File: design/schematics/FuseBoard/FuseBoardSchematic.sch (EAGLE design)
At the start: 11 parts

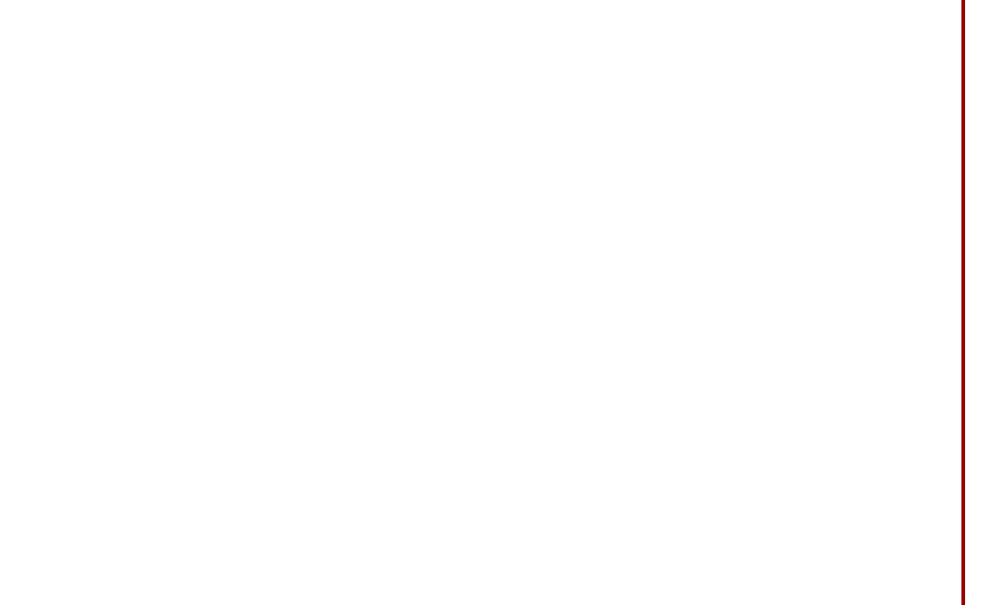
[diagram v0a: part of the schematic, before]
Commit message: Routed Fuse Board
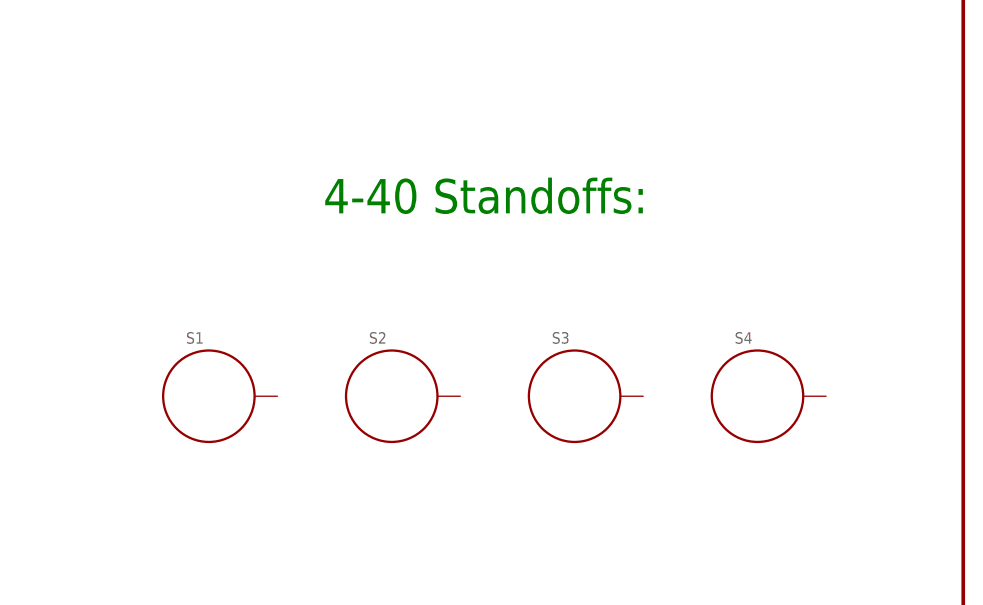
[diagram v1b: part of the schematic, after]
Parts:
- added S1, S2, S3, S4: STANDOFF_ELECTRICAL, SparkFun-Electromechanical:STANDOFF_ELECTRICAL
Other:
- note added: "4-40 Standoffs:"
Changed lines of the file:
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@@
 <part name="JETSON_FUSE" library="fuse" deviceset="SH22,5A" device="" value="2A"/>
 <part name="UIP_FUSE" library="fuse" deviceset="SH22,5A" device="" value="2A"/>
+<part name="S1" library="SparkFun-Electromechanical" deviceset="STANDOFF_ELECTRICAL" device=""/>
+<part name="S2" library="SparkFun-Electromechanical" deviceset="STANDOFF_ELECTRICAL" device=""/>
+<part name="S3" library="SparkFun-Electromechanical" deviceset="STANDOFF_ELECTRICAL" device=""/>
+<part name="S4" library="SparkFun-Electromechanical" deviceset="STANDOFF_ELECTRICAL" device=""/>
 </parts>
 <sheets>
@@
 <text x="134.62" y="190.5" size="3.81" layer="91">Power Control:</text>
 <text x="261.62" y="190.5" size="3.81" layer="91">Fuses:</text>
+<text x="360.68" y="45.72" size="3.81" layer="91">4-40 Standoffs:</text>
 </plain>
 <instances>
@@
 <instance part="JETSON_FUSE" gate="1" x="269.24" y="167.64"/>
 <instance part="UIP_FUSE" gate="1" x="269.24" y="160.02"/>
+<instance part="S1" gate="G$1" x="347.98" y="25.4"/>
+<instance part="S2" gate="G$1" x="368.3" y="25.4"/>
+<instance part="S3" gate="G$1" x="388.62" y="25.4"/>
+<instance part="S4" gate="G$1" x="408.94" y="25.4"/>
 </instances>
 <busses>

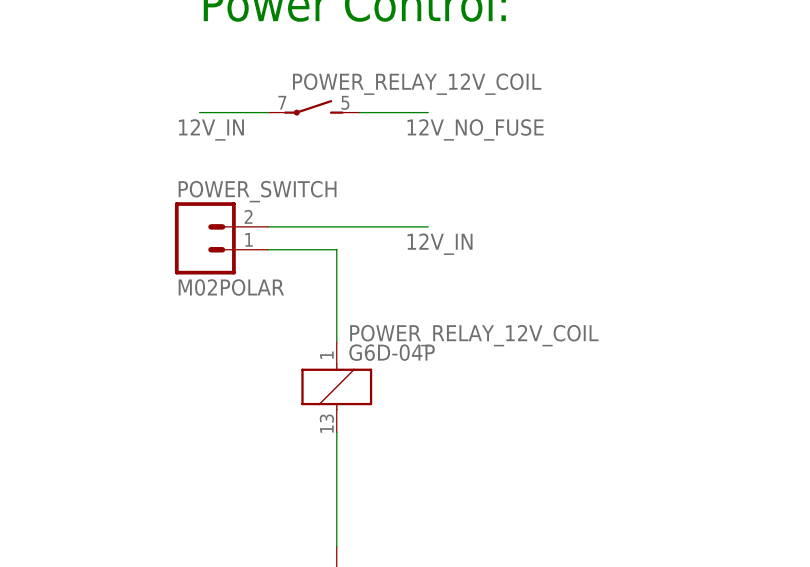
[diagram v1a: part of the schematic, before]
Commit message: Fixed routing issues and updated BOM
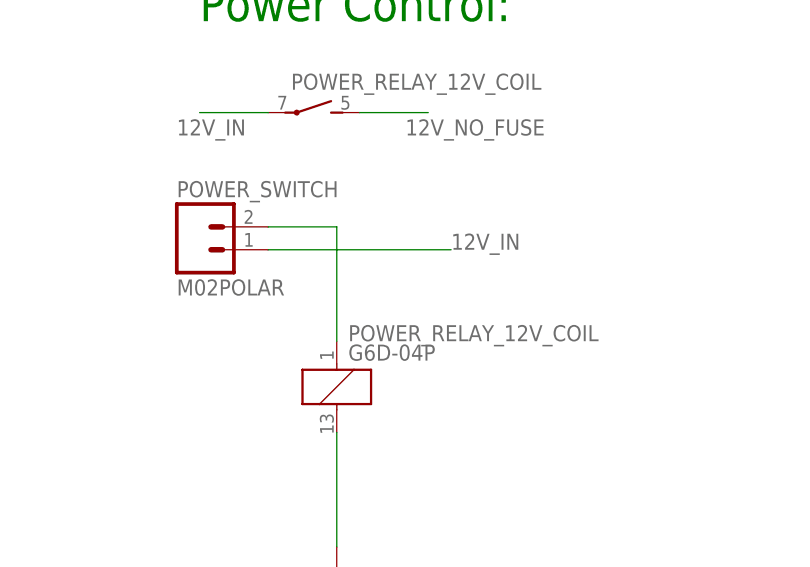
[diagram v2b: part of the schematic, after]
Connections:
- net 12V_IN: now also POWER_SWITCH.1; no longer POWER_SWITCH.2
- net N$2: now also POWER_SWITCH.2; no longer POWER_SWITCH.1
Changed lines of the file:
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@@
 </segment>
 <segment>
-<pinref part="POWER_SWITCH" gate="G$1" pin="2"/>
-<wire x1="142.24" y1="167.64" x2="160.02" y2="167.64" width="0.1524" layer="91"/>
-<label x="157.48" y="165.1" size="1.778" layer="95"/>
+<pinref part="POWER_SWITCH" gate="G$1" pin="1"/>
+<wire x1="142.24" y1="165.1" x2="162.56" y2="165.1" width="0.1524" layer="91"/>
+<label x="162.56" y="165.1" size="1.778" layer="95"/>
 </segment>
 </net>
@@
 <net name="N$2" class="0">
 <segment>
-<pinref part="POWER_SWITCH" gate="G$1" pin="1"/>
-<wire x1="149.86" y1="165.1" x2="142.24" y2="165.1" width="0.1524" layer="91"/>
 <pinref part="POWER_RELAY_12V_COIL" gate="1" pin="1"/>
-<wire x1="149.86" y1="165.1" x2="149.86" y2="154.94" width="0.1524" layer="91"/>
+<wire x1="149.86" y1="167.64" x2="149.86" y2="154.94" width="0.1524" layer="91"/>
+<pinref part="POWER_SWITCH" gate="G$1" pin="2"/>
+<wire x1="149.86" y1="167.64" x2="142.24" y2="167.64" width="0.1524" layer="91"/>
 </segment>
 </net>

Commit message: Updated fuse ratings
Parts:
- MOTOR_FUSE: value 2A -> 3A
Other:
- note added: "This schematic contains the power protection circuitry for the AGSE system. Board Functions: 1. Accepts power from either the wall or batteries 2. Power On/Off control via pluggable switch 3. A 3 Amp fuse to the motor control boards 4. A 2 Amp fuse to the jetson 5. A 2 Amp fuse to the UIP Board Mounting: 4-40 Standoffs in the corners"
- note removed: "This schematic contains the power protection circuitry for the AGSE system. Board Functions: 1. Accepts power from either the wall or batteries 2. Power On/Off control via pluggable switch 3. A TODO Amp fuse to the motor control boards 4. A TODO Amp fuse to the jetson 5. A TODO Amp fuse to the UIP Board Mounting: 4-40 Standoffs in the corners and center"
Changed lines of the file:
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@@
 <part name="POWER_RELAY_12V_COIL" library="relay" deviceset="G6D?*" device="-04P" value="G6D-04P"/>
 <part name="GND3" library="SparkFun-Aesthetics" deviceset="GND" device=""/>
-<part name="MOTOR_FUSE" library="fuse" deviceset="SH22,5A" device="" value="2A"/>
+<part name="MOTOR_FUSE" library="fuse" deviceset="SH22,5A" device="" value="3A"/>
 <part name="JETSON_FUSE" library="fuse" deviceset="SH22,5A" device="" value="2A"/>
 <part name="UIP_FUSE" library="fuse" deviceset="SH22,5A" device="" value="2A"/>
@@
 1. Accepts power from either the wall or  batteries
 2. Power On/Off control via pluggable switch
-3. A TODO Amp fuse to the motor control boards
-4. A TODO Amp fuse to the jetson
-5. A TODO Amp fuse to the UIP
+3. A 3 Amp fuse to the motor control boards
+4. A 2 Amp fuse to the jetson
+5. A 2 Amp fuse to the UIP
 Board Mounting:
-4-40 Standoffs in the corners and center</text>
+4-40 Standoffs in the corners</text>
 <text x="27.94" y="190.5" size="3.81" layer="91">Power In:</text>
 <text x="381" y="190.5" size="3.81" layer="91">Power Out:</text>

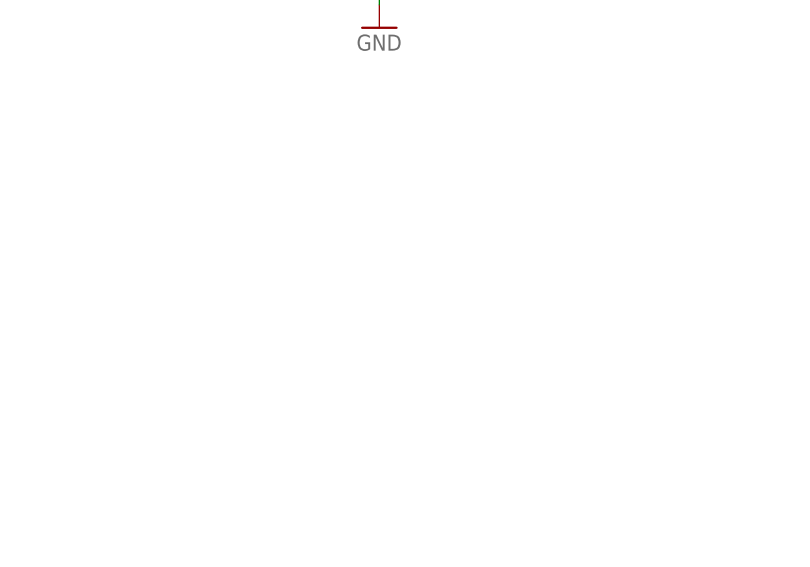
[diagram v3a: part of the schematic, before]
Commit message: Added wall power port to fuse board
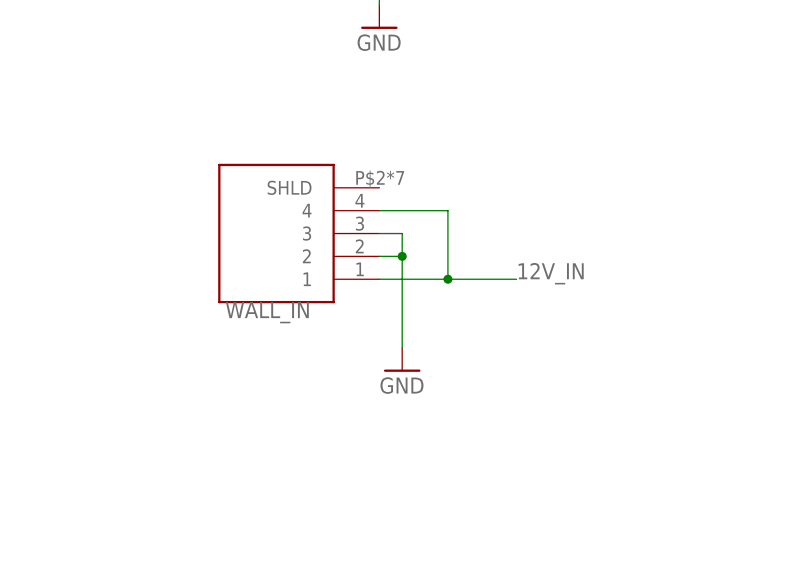
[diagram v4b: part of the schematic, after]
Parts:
- added WALL_IN: KPJX-4S-S, KPJX:KPJX-4S-S
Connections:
- net 12V_IN: now also WALL_IN.1, WALL_IN.4
- net GND: now also WALL_IN.2, WALL_IN.3
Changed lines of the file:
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@@
 <part name="S3" library="SparkFun-Electromechanical" deviceset="STANDOFF_ELECTRICAL" device=""/>
 <part name="S4" library="SparkFun-Electromechanical" deviceset="STANDOFF_ELECTRICAL" device=""/>
+<part name="WALL_IN" library="KPJX" deviceset="KPJX-4S-S" device=""/>
+<part name="GND4" library="SparkFun-Aesthetics" deviceset="GND" device=""/>
 </parts>
 <sheets>
@@
 <instance part="S3" gate="G$1" x="388.62" y="25.4"/>
 <instance part="S4" gate="G$1" x="408.94" y="25.4"/>
+<instance part="WALL_IN" gate="G$1" x="33.02" y="137.16" smashed="yes" rot="R180">
+<attribute name="NAME" x="35.56" y="132.08" size="1.778" layer="95" rot="R180"/>
+</instance>
+<instance part="GND4" gate="1" x="45.72" y="124.46"/>
 </instances>
 <busses>
@@
 <wire x1="142.24" y1="165.1" x2="162.56" y2="165.1" width="0.1524" layer="91"/>
 <label x="162.56" y="165.1" size="1.778" layer="95"/>
+</segment>
+<segment>
+<pinref part="WALL_IN" gate="G$1" pin="4"/>
+<wire x1="43.18" y1="142.24" x2="50.8" y2="142.24" width="0.1524" layer="91"/>
+<wire x1="50.8" y1="142.24" x2="50.8" y2="134.62" width="0.1524" layer="91"/>
+<pinref part="WALL_IN" gate="G$1" pin="1"/>
+<wire x1="43.18" y1="134.62" x2="50.8" y2="134.62" width="0.1524" layer="91"/>
+<wire x1="50.8" y1="134.62" x2="58.42" y2="134.62" width="0.1524" layer="91"/>
+<junction x="50.8" y="134.62"/>
+<label x="58.42" y="134.62" size="1.778" layer="95"/>
 </segment>
 </net>
@@
 <wire x1="149.86" y1="132.08" x2="149.86" y2="144.78" width="0.1524" layer="91"/>
 </segment>
+<segment>
+<pinref part="WALL_IN" gate="G$1" pin="3"/>
+<wire x1="43.18" y1="139.7" x2="45.72" y2="139.7" width="0.1524" layer="91"/>
+<pinref part="WALL_IN" gate="G$1" pin="2"/>
+<wire x1="43.18" y1="137.16" x2="45.72" y2="137.16" width="0.1524" layer="91"/>
+<wire x1="45.72" y1="137.16" x2="45.72" y2="139.7" width="0.1524" layer="91"/>
+<wire x1="45.72" y1="137.16" x2="45.72" y2="127" width="0.1524" layer="91"/>
+<junction x="45.72" y="137.16"/>
+<pinref part="GND4" gate="1" pin="GND"/>
+</segment>
 </net>
 <net name="12V_NO_FUSE" class="0">
@@
 </sheet>
 </sheets>
+<errors>
+</errors>
 </schematic>
 </drawing>
